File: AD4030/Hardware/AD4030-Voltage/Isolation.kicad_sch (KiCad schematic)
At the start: 26 parts, among them J401 Conn_01x08, J402 Conn_01x07, J403 PMOD, J404 PMOD, U401 ADuM260N, U402 ADuM260N

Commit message: Created readme.md
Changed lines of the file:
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@@
 		(dnp no)
 		(property "Reference" "R406"
-			(at 217.17 87.63 90)
+			(at 205.486 87.884 90)
 			(effects
 				(font
@@
 		(dnp no)
 		(property "Reference" "R401"
-			(at 216.662 59.944 90)
+			(at 205.232 59.944 90)
 			(effects
 				(font
@@
 		(dnp no)
 		(property "Reference" "R405"
-			(at 216.916 85.09 90)
+			(at 205.232 85.344 90)
 			(effects
 				(font
@@
 		(dnp no)
 		(property "Reference" "R402"
-			(at 216.662 62.484 90)
+			(at 205.232 62.484 90)
 			(effects
 				(font
@@
 		(dnp no)
 		(property "Reference" "R404"
-			(at 216.662 67.564 90)
+			(at 205.232 67.564 90)
 			(effects
 				(font
@@
 		(dnp no)
 		(property "Reference" "R403"
-			(at 216.662 65.024 90)
-			(effects
-				(font
+			(at 205.232 65.024 90)
+			(effects
+				(font

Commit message: Hardware design
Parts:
- removed J403, J404: PMOD, Connector_PinHeader_2.54mm:PinHeader_2x06_P2.54mm_Horizontal, symbol Connector_Generic:Conn_02x06_Top_Bottom
- added J403, J404: PMOD, Connector_PinHeader_2.54mm:PinHeader_2x06_P2.54mm_Horizontal, symbol Connector_Generic:Conn_02x06_Odd_Even
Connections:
- net GNDS: now also J403.3 (Pin_3), J403.4 (Pin_4), J404.3 (Pin_3), J404.4 (Pin_4)
- net at R410.1: now also J403.5 (Pin_5)
- net at R406.2: now also J404.10 (Pin_10)
- net at R401.2: now also J403.12 (Pin_12)
- net at R411.1: now also J404.11 (Pin_11)
- net at R405.2: now also J404.12 (Pin_12)
- net at R409.1: now also J403.7 (Pin_7)
- net at R408.1: now also J403.9 (Pin_9)
- net at R407.1: now also J403.11 (Pin_11)
- net at R404.2: now also J403.6 (Pin_6)
- net at R403.2: now also J403.8 (Pin_8)
- net at R402.2: now also J403.10 (Pin_10)
- net at R412.1: now also J404.9 (Pin_9)
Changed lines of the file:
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@@
+	)
+	(symbol
+		(lib_id "Connector_Generic:Conn_02x06_Odd_Even")
+		(at 227.33 93.98 180)
+		(unit 1)
+		(exclude_from_sim no)
+		(in_bom yes)
+		(on_board yes)
+		(dnp no)
+		(fields_autoplaced yes)
+		(property "Reference" "J404"
+			(at 226.06 80.01 0)
+			(effects
+				(font
+					(size 1.27 1.27)
+				)
+			)
+		)
+		(property "Value" "PMOD"
+			(at 226.06 82.55 0)
+			(effects
+				(font
+					(size 1.27 1.27)
+				)
+			)
+		)
+		(property "Footprint" "Connector_PinHeader_2.54mm:PinHeader_2x06_P2.54mm_Horizontal"
+			(at 227.33 93.98 0)
+			(effects
+				(font
+					(size 1.27 1.27)
+				)
+				(hide yes)
+			)
+		)
+		(property "Datasheet" "~"
+			(at 227.33 93.98 0)
+			(effects
+				(font
+					(size 1.27 1.27)
+				)
+				(hide yes)
+			)
+		)
+		(property "Description" "Generic connector, double row, 02x06, odd/even pin numbering scheme (row 1 odd numbers, row 2 even numbers), script generated (kicad-library-utils/schlib/autogen/connector/)"
+			(at 227.33 93.98 0)
+			(effects
+				(font
+					(size 1.27 1.27)
+				)
+				(hide yes)
+			)
+		)
+		(pin "4"
+		)
+		(pin "6"
+		)
+		(pin "5"
+		)
+		(pin "9"
+		)
+		(pin "10"
+		)
+		(pin "1"
+		)
+		(pin "11"
+		)
+		(pin "7"
+		)
+		(pin "2"
+		)
+		(pin "12"
+		)
+		(pin "8"
+		)
+		(pin "3"
+		)
+		(instances
+			(project "AD4030-Voltage"
+				(path "/af28bfe6-a5ae-47dd-9259-97a6edcec559/c043c7b2-3c43-41f1-9746-1c7b8c419471"
+					(reference "J404")
+					(unit 1)
+				)
+			)
+		)
 	)
 	(symbol
@@
 	)
 	(symbol
-		(lib_id "Connector_Generic:Conn_02x06_Top_Bottom")
-		(at 224.79 68.58 0)
-		(mirror x)
-		(unit 1)
-		(exclude_from_sim no)
-		(in_bom yes)
-		(on_board yes)
-		(dnp no)
-		(property "Reference" "J403"
-			(at 225.806 55.118 0)
-			(effects
-				(font
-					(size 1.27 1.27)
-				)
-			)
-		)
-		(property "Value" "PMOD"
-			(at 226.06 57.404 0)
-			(effects
-				(font
-					(size 1.27 1.27)
-				)
-			)
-		)
-		(property "Footprint" "Connector_PinHeader_2.54mm:PinHeader_2x06_P2.54mm_Horizontal"
-			(at 224.79 68.58 0)
-			(effects
-				(font
-					(size 1.27 1.27)
-				)
-				(hide yes)
-			)
-		)
-		(property "Datasheet" "~"
-			(at 224.79 68.58 0)
-			(effects
-				(font
-					(size 1.27 1.27)
-				)
-				(hide yes)
-			)
-		)
-		(property "Description" "Generic connector, double row, 02x06, top/bottom pin numbering scheme (row 1: 1...pins_per_row, row2: pins_per_row+1 ... num_pins), script generated (kicad-library-utils/schlib/autogen/connector/)"
-			(at 224.79 68.58 0)
-			(effects
-				(font
-					(size 1.27 1.27)
-				)
-				(hide yes)
-			)
-		)
-		(pin "2"
-		)
-		(pin "7"
-		)
-		(pin "9"
-		)
-		(pin "8"
-		)
-		(pin "4"
-		)
-		(pin "5"
-		)
-		(pin "3"
-		)
-		(pin "6"
-		)
-		(pin "11"
-		)
-		(pin "1"
-		)
-		(pin "10"
-		)
-		(pin "12"
-		)
-		(instances
-			(project ""
-				(path "/af28bfe6-a5ae-47dd-9259-97a6edcec559/c043c7b2-3c43-41f1-9746-1c7b8c419471"
-					(reference "J403")
-					(unit 1)
-				)
-			)
-		)
-	)
-	(symbol
 		(lib_id "AD4030:VIO")
 		(at 24.13 176.53 0)
@@
 	)
 	(symbol
+		(lib_id "Connector_Generic:Conn_02x06_Odd_Even")
+		(at 227.33 68.58 180)
+		(unit 1)
+		(exclude_from_sim no)
+		(in_bom yes)
+		(on_board yes)
+		(dnp no)
+		(fields_autoplaced yes)
+		(property "Reference" "J403"
+			(at 226.06 54.61 0)
+			(effects
+				(font
+					(size 1.27 1.27)
+				)
+			)
+		)
+		(property "Value" "PMOD"
+			(at 226.06 57.15 0)
+			(effects
+				(font
+					(size 1.27 1.27)
+				)
+			)
+		)
+		(property "Footprint" "Connector_PinHeader_2.54mm:PinHeader_2x06_P2.54mm_Horizontal"
+			(at 227.33 68.58 0)
+			(effects
+				(font
+					(size 1.27 1.27)
+				)
+				(hide yes)
+			)
+		)
+		(property "Datasheet" "~"
+			(at 227.33 68.58 0)
+			(effects
+				(font
+					(size 1.27 1.27)
+				)
+				(hide yes)
+			)
+		)
+		(property "Description" "Generic connector, double row, 02x06, odd/even pin numbering scheme (row 1 odd numbers, row 2 even numbers), script generated (kicad-library-utils/schlib/autogen/connector/)"
+			(at 227.33 68.58 0)
+			(effects
+				(font
+					(size 1.27 1.27)
+				)
+				(hide yes)
+			)
+		)
+		(pin "4"
+		)
+		(pin "6"
+		)
+		(pin "5"
+		)
+		(pin "9"
+		)
+		(pin "10"
+		)
+		(pin "1"
+		)
+		(pin "11"
+		)
+		(pin "7"
+		)
+		(pin "2"
+		)
+		(pin "12"
+		)
+		(pin "8"
+		)
+		(pin "3"
+		)
+		(instances
+			(project ""
+				(path "/af28bfe6-a5ae-47dd-9259-97a6edcec559/c043c7b2-3c43-41f1-9746-1c7b8c419471"
+					(reference "J403")
+					(unit 1)
+				)
+			)
+		)
+	)
+	(symbol
 		(lib_id "power:GNDS")
 		(at 232.41 96.52 90)
@@
 					(unit 1)
 				)
-			)
-		)
-	)
-	(symbol
-		(lib_id "Connector_Generic:Conn_02x06_Top_Bottom")
-		(at 224.79 93.98 0)
-		(mirror x)
-		(unit 1)
-		(exclude_from_sim no)
-		(in_bom yes)
-		(on_board yes)
-		(dnp no)
-		(property "Reference" "J404"
-			(at 226.06 81.534 0)
-			(effects
-				(font
-					(size 1.27 1.27)
-				)
-			)
-		)
-		(property "Value" "PMOD"
-			(at 226.06 83.566 0)
-			(effects
-				(font
-					(size 1.27 1.27)
-				)
-			)
-		)
-		(property "Footprint" "Connector_PinHeader_2.54mm:PinHeader_2x06_P2.54mm_Horizontal"
-			(at 224.79 93.98 0)
-			(effects
-				(font
-					(size 1.27 1.27)
-				)
-				(hide yes)
-			)
-		)
-		(property "Datasheet" "~"
-			(at 224.79 93.98 0)
-			(effects
-				(font
-					(size 1.27 1.27)
-				)
-				(hide yes)
-			)
-		)
-		(property "Description" "Generic connector, double row, 02x06, top/bottom pin numbering scheme (row 1: 1...pins_per_row, row2: pins_per_row+1 ... num_pins), script generated (kicad-library-utils/schlib/autogen/connector/)"
-			(at 224.79 93.98 0)
-			(effects
-				(font
-					(size 1.27 1.27)
-				)
-				(hide yes)
-			)
-		)
-		(pin "2"
-		)
-		(pin "7"
-		)
-		(pin "9"
-		)
-		(pin "8"
-		)
-		(pin "4"
-		)
-		(pin "5"
-		)
-		(pin "3"
-		)
-		(pin "6"
-		)
-		(pin "11"
-		)
-		(pin "1"
-		)
-		(pin "10"
-		)
-		(pin "12"
-		)
-		(instances
-			(project "AD4030-Voltage"
-				(path "/af28bfe6-a5ae-47dd-9259-97a6edcec559/c043c7b2-3c43-41f1-9746-1c7b8c419471"
-					(reference "J404")
-					(unit 1)
-				)

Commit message: Hardware design
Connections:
- net ADC_BUSY: now also U401.7 (VIF); no longer U401.6 (VIE)
- net ADC_SDO0: now also U401.3 (VIB); no longer U401.2 (VIA)
- net ADC_SDO1: now also U401.4 (VIC); no longer U401.3 (VIB)
- net ADC_SDO2: now also U401.5 (VID); no longer U401.4 (VIC)
- net ADC_SDO3: now also U401.6 (VIE); no longer U401.5 (VID)
- net CLK_100MHz: now also U401.2 (VIA); no longer U401.7 (VIF)
- net CONN_100MHz: now also J401.1 (Pin_1), U401.15 (VOA); no longer J401.6 (Pin_6), U401.10 (VOF)
- net CONN_BUSY: now also J401.6 (Pin_6), U401.10 (VOF); no longer J401.5 (Pin_5), U401.11 (VOE)
- net CONN_SDO0: now also J401.2 (Pin_2), U401.14 (VOB); no longer J401.1 (Pin_1), U401.15 (VOA)
- net CONN_SDO1: now also J401.3 (Pin_3), U401.13 (VOC); no longer J401.2 (Pin_2), U401.14 (VOB)
- net CONN_SDO2: now also J401.4 (Pin_4), U401.12 (VOD); no longer J401.3 (Pin_3), U401.13 (VOC)
- net CONN_SDO3: now also J401.5 (Pin_5), U401.11 (VOE); no longer J401.4 (Pin_4), U401.12 (VOD)
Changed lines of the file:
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@@
 	)
 	(label "CONN_SDO1"
-		(at 133.35 63.5 0)
+		(at 133.35 66.04 0)
 		(fields_autoplaced yes)
 		(effects
@@
 	)
 	(label "CONN_SDO3"
-		(at 133.35 68.58 0)
+		(at 133.35 71.12 0)
 		(fields_autoplaced yes)
 		(effects
@@
 	)
 	(label "CONN_SDO0"
-		(at 133.35 60.96 0)
+		(at 133.35 63.5 0)
 		(fields_autoplaced yes)
 		(effects
@@
 	)
 	(label "CONN_SDO2"
-		(at 133.35 66.04 0)
+		(at 133.35 68.58 0)
 		(fields_autoplaced yes)
 		(effects
@@
 	)
 	(label "CONN_BUSY"
-		(at 133.35 71.12 0)
+		(at 133.35 73.66 0)
 		(fields_autoplaced yes)
 		(effects
@@
 	)
 	(label "CONN_100MHz"
-		(at 133.35 73.66 0)
+		(at 133.35 60.96 0)
 		(fields_autoplaced yes)
 		(effects
@@
 	(hierarchical_label "CLK_100MHz"
 		(shape input)
+		(at 71.12 63.5 180)
+		(fields_autoplaced yes)
+		(effects
+			(font
+				(size 1.27 1.27)
+			)
+			(justify right)
+		)
+	)
+	(hierarchical_label "ADC_SDO0"
+		(shape input)
+		(at 71.12 66.04 180)
+		(fields_autoplaced yes)
+		(effects
+			(font
+				(size 1.27 1.27)
+			)
+			(justify right)
+		)
+	)
+	(hierarchical_label "ADC_SCK"
+		(shape output)
+		(at 71.12 107.95 180)
+		(fields_autoplaced yes)
+		(effects
+			(font
+				(size 1.27 1.27)
+			)
+			(justify right)
+		)
+	)
+	(hierarchical_label "Gain_x10"
+		(shape output)
+		(at 71.12 115.57 180)
+		(fields_autoplaced yes)
+		(effects
+			(font
+				(size 1.27 1.27)
+			)
+			(justify right)
+		)
+	)
+	(hierarchical_label "ADC_SDO3"
+		(shape input)
+		(at 71.12 73.66 180)
+		(fields_autoplaced yes)
+		(effects
+			(font
+				(size 1.27 1.27)
+			)
+			(justify right)
+		)
+	)
+	(hierarchical_label "ADC_SDO1"
+		(shape input)
+		(at 71.12 68.58 180)
+		(fields_autoplaced yes)
+		(effects
+			(font
+				(size 1.27 1.27)
+			)
+			(justify right)
+		)
+	)
+	(hierarchical_label "ADC_SDO2"
+		(shape input)
+		(at 71.12 71.12 180)
+		(fields_autoplaced yes)
+		(effects
+			(font
+				(size 1.27 1.27)
+			)
+			(justify right)
+		)
+	)
+	(hierarchical_label "ADC_~{CS}"
+		(shape output)
+		(at 71.12 102.87 180)
+		(fields_autoplaced yes)
+		(effects
+			(font
+				(size 1.27 1.27)
+			)
+			(justify right)
+		)
+	)
+	(hierarchical_label "ADC_CNV"
+		(shape output)
+		(at 71.12 110.49 180)
+		(fields_autoplaced yes)
+		(effects
+			(font
+				(size 1.27 1.27)
+			)
+			(justify right)
+		)
+	)
+	(hierarchical_label "ADC_SDI"
+		(shape output)
+		(at 71.12 105.41 180)
+		(fields_autoplaced yes)
+		(effects
+			(font
+				(size 1.27 1.27)
+			)
+			(justify right)
+		)
+	)
+	(hierarchical_label "ADC_BUSY"
+		(shape input)
 		(at 71.12 76.2 180)
 		(fields_autoplaced yes)
 		(effects
-			(font
-				(size 1.27 1.27)
-			)
-			(justify right)
-		)
-	)
-	(hierarchical_label "ADC_SDO0"
-		(shape input)
-		(at 71.12 63.5 180)
-		(fields_autoplaced yes)
-		(effects
-			(font
-				(size 1.27 1.27)
-			)
-			(justify right)
-		)
-	)
-	(hierarchical_label "ADC_SCK"
-		(shape output)
-		(at 71.12 107.95 180)
-		(fields_autoplaced yes)
-		(effects
-			(font
-				(size 1.27 1.27)
-			)
-			(justify right)
-		)
-	)
-	(hierarchical_label "Gain_x10"
-		(shape output)
-		(at 71.12 115.57 180)
-		(fields_autoplaced yes)
-		(effects
-			(font
-				(size 1.27 1.27)
-			)
-			(justify right)
-		)
-	)
-	(hierarchical_label "ADC_SDO3"
-		(shape input)
-		(at 71.12 71.12 180)
-		(fields_autoplaced yes)
-		(effects
-			(font
-				(size 1.27 1.27)
-			)
-			(justify right)
-		)
-	)
-	(hierarchical_label "ADC_SDO1"
-		(shape input)
-		(at 71.12 66.04 180)
-		(fields_autoplaced yes)
-		(effects
-			(font
-				(size 1.27 1.27)
-			)
-			(justify right)
-		)
-	)
-	(hierarchical_label "ADC_SDO2"
-		(shape input)
-		(at 71.12 68.58 180)
-		(fields_autoplaced yes)
-		(effects
-			(font
-				(size 1.27 1.27)
-			)
-			(justify right)
-		)
-	)
-	(hierarchical_label "ADC_~{CS}"
-		(shape output)
-		(at 71.12 102.87 180)
-		(fields_autoplaced yes)
-		(effects
-			(font
-				(size 1.27 1.27)
-			)
-			(justify right)
-		)
-	)
-	(hierarchical_label "ADC_CNV"
-		(shape output)
-		(at 71.12 110.49 180)
-		(fields_autoplaced yes)
-		(effects
-			(font
-				(size 1.27 1.27)
-			)
-			(justify right)
-		)
-	)
-	(hierarchical_label "ADC_SDI"
-		(shape output)
-		(at 71.12 105.41 180)
-		(fields_autoplaced yes)
-		(effects
-			(font
-				(size 1.27 1.27)
-			)
-			(justify right)
-		)
-	)
-	(hierarchical_label "ADC_BUSY"
-		(shape input)
-		(at 71.12 73.66 180)
-		(fields_autoplaced yes)
-		(effects

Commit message: PCB layout
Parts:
- renumbered R402 to R401, R403 to R402, R404 to R403, R405 to R404, R406 to R405, R401 to R406, R408 to R407, R409 to R408, R410 to R409, R411 to R410, R412 to R411, R407 to R412
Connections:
- net ADC_CNV: now also U402.10 (VOF); no longer U402.12 (VOD)
- net ADC_SCK: now also U402.11 (VOE); no longer U402.13 (VOC)
- net ADC_SDI: now also U402.12 (VOD); no longer U402.14 (VOB)
- net ADC_SDO0: now also U401.6 (VIE); no longer U401.3 (VIB)
- net ADC_SDO3: now also U401.3 (VIB); no longer U401.6 (VIE)
- net ADC_~{CS}: now also U402.13 (VOC); no longer U402.15 (VOA)
- net CONN_100MHz: now also R403.1; no longer R408.2
- net CONN_BUSY: now also R407.2; no longer R402.1
- net CONN_CNV: now also J401.7 (Pin_7), R406.1, U402.7 (VIF); no longer J402.2 (Pin_2), R405.1, U402.5 (VID)
- net CONN_GAIN_x10: now also R410.2, U402.2 (VIA); no longer R411.2, U402.7 (VIF)
- net CONN_GAIN_x20: now also R404.1, U402.3 (VIB); no longer R410.2, U402.6 (VIE)
- net CONN_SCK: now also J401.8 (Pin_8), R412.2, U402.6 (VIE); no longer J402.1 (Pin_1), R404.1, U402.4 (VIC)
- net CONN_SDI: now also J402.1 (Pin_1), R405.1, U402.5 (VID); no longer J401.8 (Pin_8), R409.2, U402.3 (VIB)
- net CONN_SDO0: now also J401.5 (Pin_5), R401.1, U401.11 (VOE); no longer J401.2 (Pin_2), R406.1, U401.14 (VOB)
- net CONN_SDO1: now also R402.1; no longer R412.2
- net CONN_SDO2: now also R408.2; no longer R401.1
- net CONN_SDO3: now also J401.2 (Pin_2), R409.2, U401.14 (VOB); no longer J401.5 (Pin_5), R407.2, U401.11 (VOE)
- net CONN_~{CS}: now also J402.2 (Pin_2), R411.2, U402.4 (VIC); no longer J401.7 (Pin_7), R403.1, U402.2 (VIA)
- net GAIN_x20: now also U402.14 (VOB); no longer U402.11 (VOE)
- net Gain_x10: now also U402.15 (VOA); no longer U402.10 (VOF)
- net at R405.2: now also J404.8 (Pin_8); no longer J404.10 (Pin_10)
- net at R406.2: now also J404.6 (Pin_6); no longer J403.12 (Pin_12)
- net at R410.1: now also J404.9 (Pin_9); no longer J404.11 (Pin_11)
- net at R404.2: now also J404.10 (Pin_10); no longer J404.12 (Pin_12)
- net at J404.5 (Pin_5): now also R412.1
- net at J404.7 (Pin_7): now also R411.1
- net at J403.11 (Pin_11): no longer R412.1
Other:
- moved on the sheet: J401, J402, R404, R405, R406, R410, R411, R412

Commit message: PCB layout
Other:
- moved on the sheet: C401, C402, C403, C404, C405, C406, C407, C408, J401, J402, J403, J404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

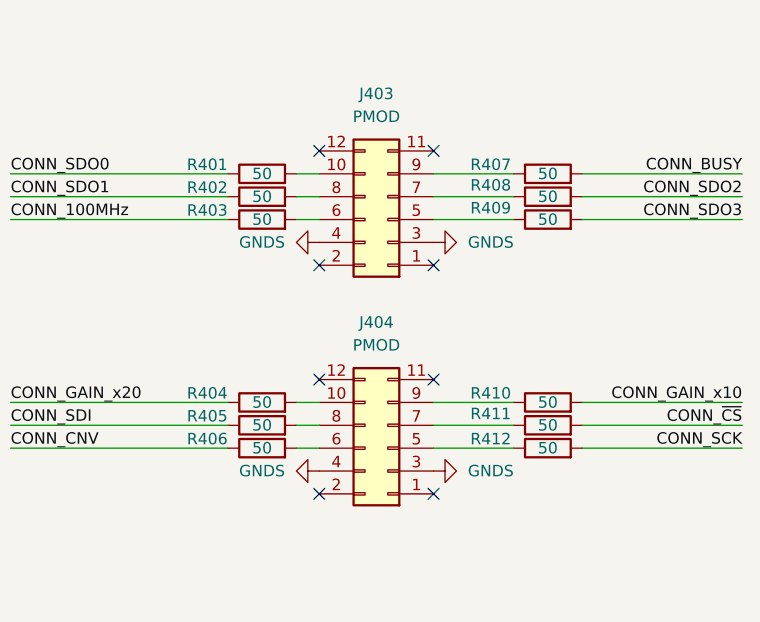
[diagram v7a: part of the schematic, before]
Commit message: AD4030-Voltage : Ordered BOM
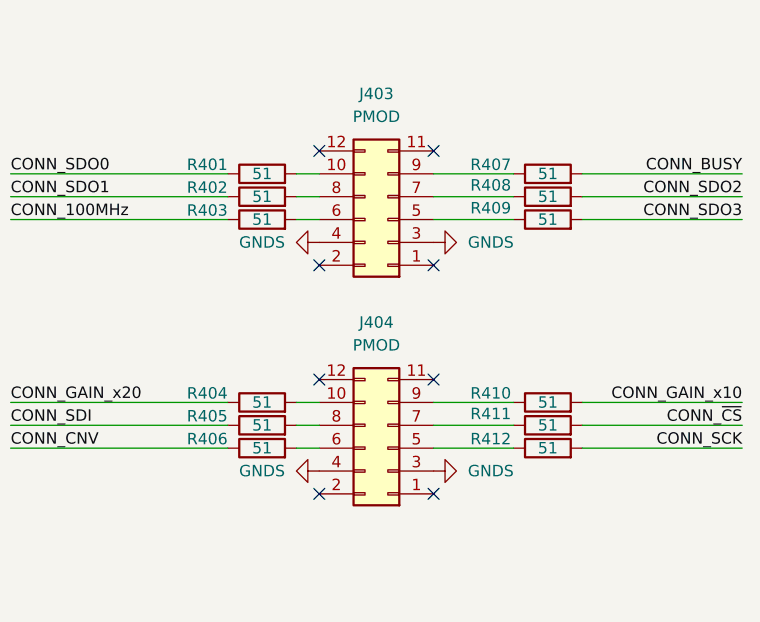
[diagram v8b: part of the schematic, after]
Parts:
- R401, R402, R403, R404, R405, R406, R407, R408, R409, R410, R411, R412: value 50 -> 51
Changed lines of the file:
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@@
 			)
 		)
-		(property "Value" "50"
+		(property "Value" "51"
 			(at 255.27 68.58 90)
 			(effects
@@
 			)
 		)
-		(property "Value" "50"
+		(property "Value" "51"
 			(at 223.52 91.44 90)
 			(effects
@@
 			)
 		)
-		(property "Value" "50"
+		(property "Value" "51"
 			(at 223.52 93.98 90)
 			(effects
@@
 			)
 		)
-		(property "Value" "50"
+		(property "Value" "51"
 			(at 255.27 88.9 90)
 			(effects
@@
 			)
 		)
-		(property "Value" "50"
+		(property "Value" "51"
 			(at 223.52 88.9 90)
 			(effects
@@
 			)
 		)
-		(property "Value" "50"
+		(property "Value" "51"
 			(at 255.27 91.44 90)
 			(effects
@@
 			)
 		)
-		(property "Value" "50"
+		(property "Value" "51"
 			(at 223.52 63.5 90)
 			(effects
@@
 			)
 		)
-		(property "Value" "50"
+		(property "Value" "51"
 			(at 223.52 68.58 90)
 			(effects
@@
 			)
 		)
-		(property "Value" "50"
+		(property "Value" "51"
 			(at 255.27 93.98 90)
 			(effects
@@
 			)
 		)
-		(property "Value" "50"
+		(property "Value" "51"
 			(at 223.52 66.04 90)
 			(effects
@@
 			)
 		)
-		(property "Value" "50"
+		(property "Value" "51"
 			(at 255.27 66.04 90)
 			(effects
@@
 			)
 		)
-		(property "Value" "50"
+		(property "Value" "51"
 			(at 255.27 63.5 90)
 			(effects
